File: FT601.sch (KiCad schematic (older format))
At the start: 23 parts, among them U1 FT601, U2 ESD7016, U4 ECP5, U5 Si5351, X1 GSB443133HR, Y1 FL3000027, Y2 ABM11-141-26.000MHZ

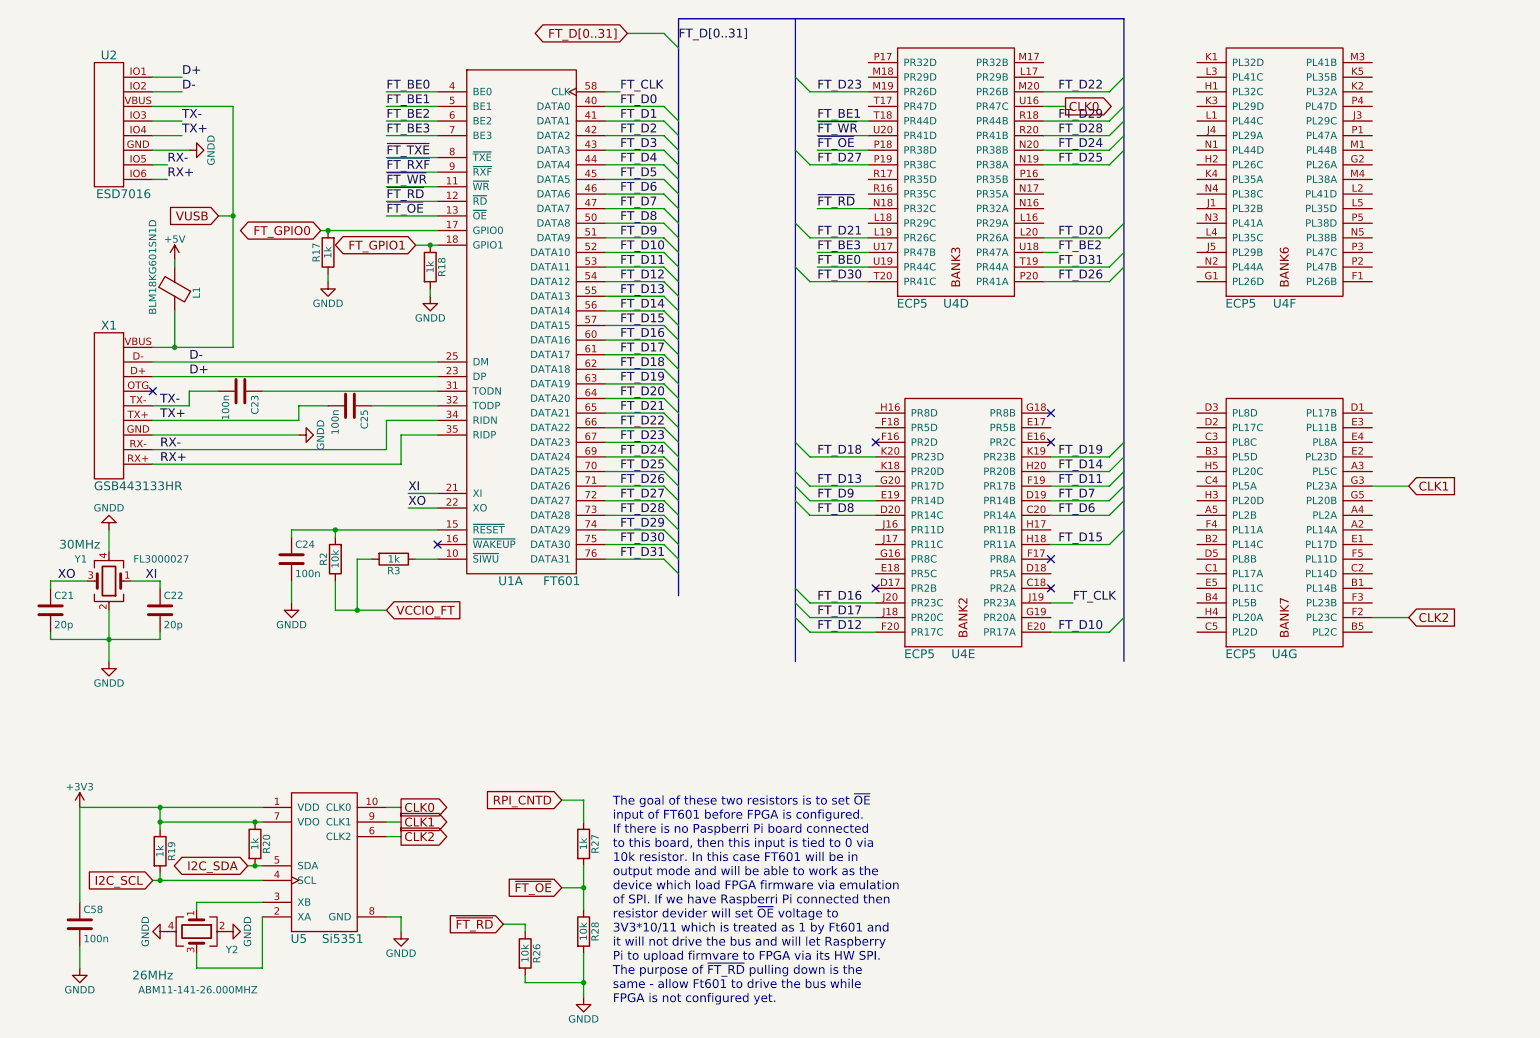
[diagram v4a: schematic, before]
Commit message: Caps for FPGA are placed. Most of FPGA power is traced. Need to trace Rpi connector
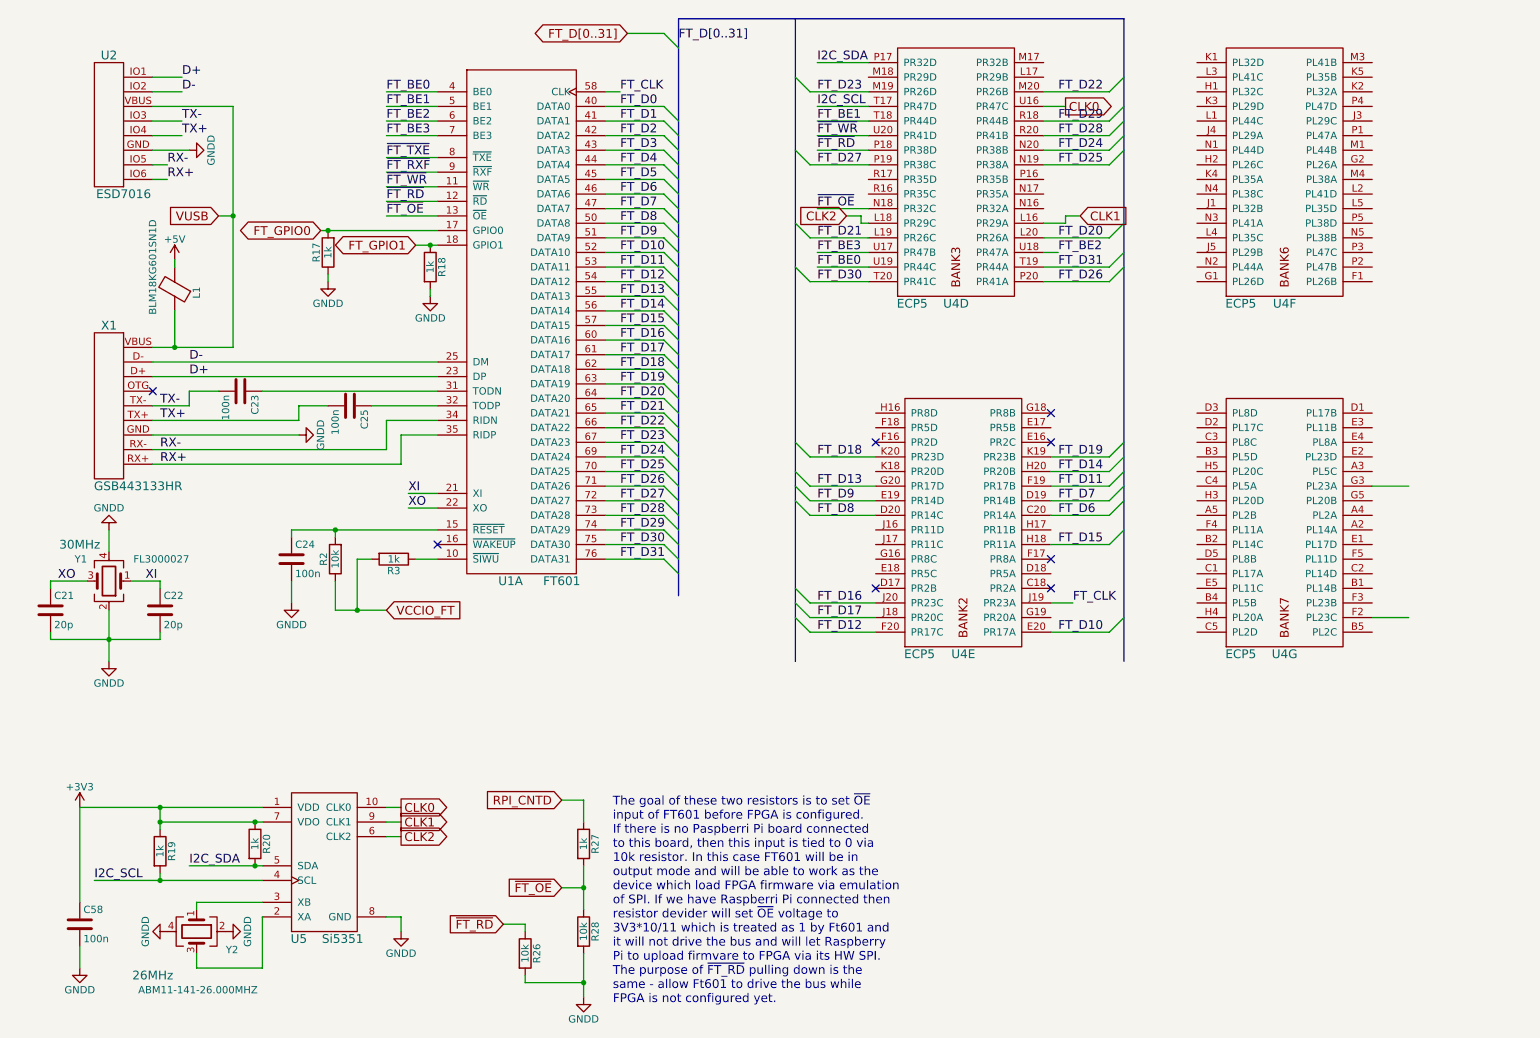
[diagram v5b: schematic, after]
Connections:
- net CLK1: now also U4.L16 (PR29A); no longer U4.G3 (PL23A)
- net CLK2: now also U4.L18 (PR29C); no longer U4.F2 (PL23C)
- net I2C_SCL: now also U4.T17 (PR47D)
- net I2C_SDA: now also U4.P17 (PR32D)
- net ~FT_OE: now also U4.N18 (PR32C); no longer U4.P18 (PR38D)
- net ~FT_RD: now also U4.P18 (PR38D); no longer U4.N18 (PR32C)
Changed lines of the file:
@@
 $EndComp
 $Comp
-L GNDD #PWR043
+L GNDD #PWR044
 U 1 1 58981141
 P 2550 3650
-F 0 "#PWR043" H 2550 3400 50  0001 C CNN
+F 0 "#PWR044" H 2550 3400 50  0001 C CNN
 F 1 "GNDD" H 2550 3500 50  0000 C CNN
 F 2 "" H 2550 3650 50  0000 C CNN
@@
 TX+
 $Comp
-L GNDD #PWR044
+L GNDD #PWR045
 U 1 1 58982448
 P 1800 1700
-F 0 "#PWR044" H 1800 1450 50  0001 C CNN
+F 0 "#PWR045" H 1800 1450 50  0001 C CNN
 F 1 "GNDD" H 1800 1550 50  0000 C CNN
 F 2 "" H 1800 1700 50  0000 C CNN
@@
 $EndComp
 $Comp
-L GNDD #PWR045
+L GNDD #PWR046
 U 1 1 58983172
 P 2500 4800
-F 0 "#PWR045" H 2500 4550 50  0001 C CNN
+F 0 "#PWR046" H 2500 4550 50  0001 C CNN
 F 1 "GNDD" H 2500 4650 50  0000 C CNN
 F 2 "" H 2500 4800 50  0000 C CNN
@@
 $EndComp
 $Comp
-L GNDD #PWR046
+L GNDD #PWR047
 U 1 1 58983AFE
 P 1250 5200
-F 0 "#PWR046" H 1250 4950 50  0001 C CNN
+F 0 "#PWR047" H 1250 4950 50  0001 C CNN
 F 1 "GNDD" H 1250 5050 50  0000 C CNN
 F 2 "" H 1250 5200 50  0000 C CNN
@@
 $EndComp
 $Comp
-L GNDD #PWR047
+L GNDD #PWR048
 U 1 1 58983B6B
 P 1250 4300
-F 0 "#PWR047" H 1250 4050 50  0001 C CNN
+F 0 "#PWR048" H 1250 4050 50  0001 C CNN
 F 1 "GNDD" H 1250 4150 50  0000 C CNN
 F 2 "" H 1250 4300 50  0000 C CNN
@@
 $EndComp
 $Comp
-L GNDD #PWR048
+L GNDD #PWR049
 U 1 1 58A3CED9
 P 3450 2700
-F 0 "#PWR048" H 3450 2450 50  0001 C CNN
+F 0 "#PWR049" H 3450 2450 50  0001 C CNN
 F 1 "GNDD" H 3450 2550 50  0000 C CNN
 F 2 "" H 3450 2700 50  0000 C CNN
@@
 $EndComp
 $Comp
-L GNDD #PWR049
+L GNDD #PWR050
 U 1 1 58A3CF07
 P 2750 2600
-F 0 "#PWR049" H 2750 2350 50  0001 C CNN
+F 0 "#PWR050" H 2750 2350 50  0001 C CNN
 F 1 "GNDD" H 2750 2450 50  0000 C CNN
 F 2 "" H 2750 2600 50  0000 C CNN
@@
 $EndComp
 $Comp
-L +3V3 #PWR050
+L +3V3 #PWR051
 U 1 1 58A3E1D8
 P 1050 6200
-F 0 "#PWR050" H 1050 6050 50  0001 C CNN
+F 0 "#PWR051" H 1050 6050 50  0001 C CNN
 F 1 "+3V3" H 1050 6340 50  0000 C CNN
 F 2 "" H 1050 6200 50  0000 C CNN
@@
 $EndComp
 $Comp
-L GNDD #PWR051
+L GNDD #PWR052
 U 1 1 58A3E3AE
 P 1050 7300
-F 0 "#PWR051" H 1050 7050 50  0001 C CNN
+F 0 "#PWR052" H 1050 7050 50  0001 C CNN
 F 1 "GNDD" H 1050 7150 50  0000 C CNN
 F 2 "" H 1050 7300 50  0000 C CNN
@@
 $EndComp
 $Comp
-L GNDD #PWR052
+L GNDD #PWR053
 U 1 1 58A3F555
 P 2050 7050
-F 0 "#PWR052" H 2050 6800 50  0001 C CNN
+F 0 "#PWR053" H 2050 6800 50  0001 C CNN
 F 1 "GNDD" H 2050 6900 50  0000 C CNN
 F 2 "" H 2050 7050 50  0000 C CNN
@@
 	0    -1   -1   0
 $EndComp
-Text GLabel 1550 6700 0    60   Input ~ 0
-I2C_SCL
-Text GLabel 2200 6600 0    60   BiDi ~ 0
-I2C_SDA
 $Comp
 L R R20
@@
 CLK2
 $Comp
-L GNDD #PWR053
+L GNDD #PWR054
 U 1 1 58A415AA
 P 3250 7050
-F 0 "#PWR053" H 3250 6800 50  0001 C CNN
+F 0 "#PWR054" H 3250 6800 50  0001 C CNN
 F 1 "GNDD" H 3250 6900 50  0000 C CNN
 F 2 "" H 3250 7050 50  0000 C CNN
@@
 $EndComp
 $Comp
-L +5V #PWR054
+L +5V #PWR055
 U 1 1 58A3FC7D
 P 1700 2450
-F 0 "#PWR054" H 1700 2300 50  0001 C CNN
+F 0 "#PWR055" H 1700 2300 50  0001 C CNN
 F 1 "+5V" H 1700 2590 50  0000 C CNN
 F 2 "" H 1700 2450 50  0000 C CNN
@@
 	2300 7300 2300 6950
 Wire Wire Line
-	2200 6600 2300 6600
+	1800 6600 2300 6600
 Connection ~ 2250 6600
 Wire Wire Line
-	1550 6700 2300 6700
+	1150 6700 2300 6700
 Wire Wire Line
 	1600 6700 1600 6650
@@
 	1050 6200 1050 6850
 $Comp
-L GNDD #PWR055
+L GNDD #PWR056
 U 1 1 58A3F51F
 P 1650 7050
-F 0 "#PWR055" H 1650 6800 50  0001 C CNN
+F 0 "#PWR056" H 1650 6800 50  0001 C CNN
 F 1 "GNDD" H 1650 6900 50  0000 C CNN
 F 2 "" H 1650 7050 50  0000 C CNN
@@
 ~FT_OE
 $Comp
-L GNDD #PWR056
+L GNDD #PWR057
 U 1 1 58ABB46B
 P 4500 7500
-F 0 "#PWR056" H 4500 7250 50  0001 C CNN
+F 0 "#PWR057" H 4500 7250 50  0001 C CNN
 F 1 "GNDD" H 4500 7350 50  0000 C CNN
 F 2 "" H 4500 7500 50  0000 C CNN
@@
 Wire Wire Line
 	9900 4900 10150 4900
-Text GLabel 10150 4000 2    60   Input ~ 0
+Text GLabel 6300 2150 0    60   Input ~ 0
+CLK2
+Text GLabel 7900 2150 2    60   Input ~ 0
 CLK1
-Text GLabel 10150 4900 2    60   Input ~ 0
-CLK2
 Wire Wire Line
 	1050 6200 2300 6200
@@
 Wire Wire Line
 	6450 2400 6100 2400
+Text Label 6100 2100 0    60   ~ 0
+~FT_OE
+Wire Wire Line
+	6450 1700 6100 1700
 Text Label 6100 1700 0    60   ~ 0
-~FT_OE
-Wire Wire Line
-	6450 1700 6100 1700
-Text Label 6100 2100 0    60   ~ 0
 ~FT_RD
 Wire Wire Line
@@
 NoConn ~ 7700 3700
 NoConn ~ 7700 4700
+Text Label 1800 6600 0    60   ~ 0
+I2C_SDA
+Text Label 1150 6700 0    60   ~ 0
+I2C_SCL
+Text Label 6100 1100 0    60   ~ 0
+I2C_SDA
+Text Label 6100 1400 0    60   ~ 0
+I2C_SCL
+Wire Wire Line
+	6100 1100 6450 1100
+Wire Wire Line
+	6450 1400 6100 1400
+Wire Wire Line
+	7650 2200 7800 2200
+Wire Wire Line
+	7800 2200 7800 2150
+Wire Wire Line
+	7800 2150 7900 2150
+Wire Wire Line
+	6300 2150 6400 2150
+Wire Wire Line
+	6400 2150 6400 2200
+Wire Wire Line
+	6400 2200 6450 2200
 $EndSCHEMATC

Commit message: All traced except Rpi and LMS
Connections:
- net I2C_SCL: no longer U4.T17 (PR47D)
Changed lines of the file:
@@
 Text Label 6100 1100 0    60   ~ 0
 I2C_SDA
-Text Label 6100 1400 0    60   ~ 0
+Text Label 5350 1600 0    60   ~ 0
 I2C_SCL
 Wire Wire Line
 	6100 1100 6450 1100
 Wire Wire Line
-	6450 1400 6100 1400
-Wire Wire Line
 	7650 2200 7800 2200

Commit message: RPI is almost finished
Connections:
- net RPI_D13: now reaches U4.E17 (PR5B)
- net RPI_A5: now reaches U4.F18 (PR5D)
- net ~RPI_WE: now reaches U4.G16 (PR8C)
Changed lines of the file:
@@
 Wire Wire Line
 	6400 2200 6450 2200
+Text Label 7750 3600 0    60   ~ 0
+RPI_D13
+Text GLabel 9950 6200 0    60   BiDi ~ 0
+RPI_D[0..17]
+Entry Wire Line
+	10100 6200 10200 6100
+Text Label 10250 6100 0    60   ~ 0
+RPI_D[0..17]
+Wire Wire Line
+	10100 6200 9950 6200
+Wire Bus Line
+	10200 6100 10600 6100
+Wire Wire Line
+	7700 3600 8100 3600
+Entry Wire Line
+	8100 3600 8200 3500
+Text Label 6100 3600 0    60   ~ 0
+RPI_A5
+Text GLabel 9950 5750 0    60   BiDi ~ 0
+RPI_A[0..5]
+Entry Wire Line
+	10100 5750 10200 5650
+Text Label 10250 5650 0    60   ~ 0
+RPI_A[0..5]
+Wire Wire Line
+	10100 5750 9950 5750
+Wire Bus Line
+	10200 5650 10600 5650
+Wire Wire Line
+	6500 3600 6100 3600
+Text GLabel 6400 4500 0    60   Input ~ 0
+~RPI_WE
+Wire Wire Line
+	6500 4500 6400 4500
 $EndSCHEMATC

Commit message: Everything is done except LMS and RF
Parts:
- removed unit 6 of U4
- removed unit 7 of U4
- added unit 10 of U4
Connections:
- net ~RPI_WE is gone; now on net RPI_A5: U4.G16 (PR8C)
- net I2C_SCL: now also U4.Y2 (PB9B)
- net RPI_A5: no longer U4.F18 (PR5D)
- new net ~RPI_OE: U4.F18 (PR5D)
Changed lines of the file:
@@
 Wire Wire Line
 	4100 7000 3950 7000
-$Comp
-L ECP5 U4
-U 6 1 58ABE791
-P 8900 2700
-F 0 "U4" H 9300 2650 60  0000 C CNN
-F 1 "ECP5" H 9000 2650 60  0000 C CNN
-F 2 "sdr-foots:ECP5_381" H 7350 3250 60  0001 C CNN
-F 3 "" H 7350 3250 60  0001 C CNN
-	6    8900 2700
-	1    0    0    -1
-$EndComp
-$Comp
-L ECP5 U4
-U 7 1 58ABE82A
-P 8900 5100
-F 0 "U4" H 9300 5050 60  0000 C CNN
-F 1 "ECP5" H 9000 5050 60  0000 C CNN
-F 2 "sdr-foots:ECP5_381" H 7350 5650 60  0001 C CNN
-F 3 "" H 7350 5650 60  0001 C CNN
-	7    8900 5100
-	1    0    0    -1
-$EndComp
-Wire Wire Line
-	9900 4000 10150 4000
-Wire Wire Line
-	9900 4900 10150 4900
 Text GLabel 6300 2150 0    60   Input ~ 0
 CLK2
@@
 Text Label 6100 1100 0    60   ~ 0
 I2C_SDA
-Text Label 5350 1600 0    60   ~ 0
+Text Label 8750 1300 0    60   ~ 0
 I2C_SCL
 Wire Wire Line
@@
 Entry Wire Line
 	8100 3600 8200 3500
-Text Label 6100 3600 0    60   ~ 0
-RPI_A5
 Text GLabel 9950 5750 0    60   BiDi ~ 0
 RPI_A[0..5]
@@
 Wire Bus Line
 	10200 5650 10600 5650
-Wire Wire Line
-	6500 3600 6100 3600
-Text GLabel 6400 4500 0    60   Input ~ 0
-~RPI_WE
-Wire Wire Line
-	6500 4500 6400 4500
+Text Label 6100 4500 0    60   ~ 0
+RPI_A5
+Wire Wire Line
+	6100 4500 6500 4500
+Text GLabel 6450 3600 0    60   Input ~ 0
+~RPI_OE
+Wire Wire Line
+	6500 3600 6450 3600
+$Comp
+L ECP5 U4
+U 10 1 58C29E50
+P 9350 1500
+F 0 "U4" H 9750 1450 60  0000 C CNN
+F 1 "ECP5" H 9450 1450 60  0000 C CNN
+F 2 "sdr-foots:ECP5_381" H 7800 2050 60  0001 C CNN
+F 3 "" H 7800 2050 60  0001 C CNN
+	10   9350 1500
+	1    0    0    -1
+$EndComp
+Wire Wire Line
+	9150 1300 8750 1300
 $EndSCHEMATC
